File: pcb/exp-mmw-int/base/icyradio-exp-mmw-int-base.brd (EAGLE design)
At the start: 85.7 x 98.4 mm, 22 parts, among them U1 ATSAMD20E16A-M, U3 24AA02XX-X/OT

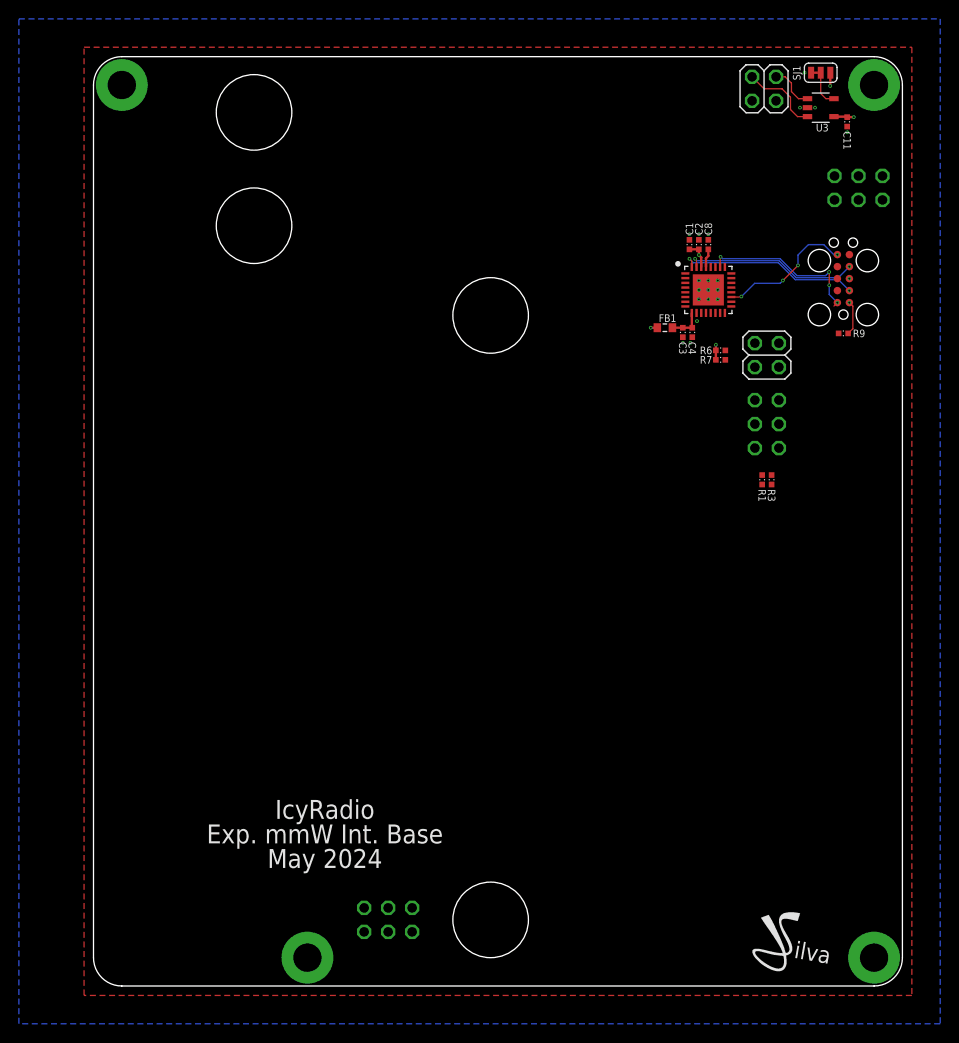
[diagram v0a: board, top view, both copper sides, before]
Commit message: pcb: Finish mmWave integrated expansion PCBs for production
Signed-off-by: João Silva <jgc3silva@gmail.com>
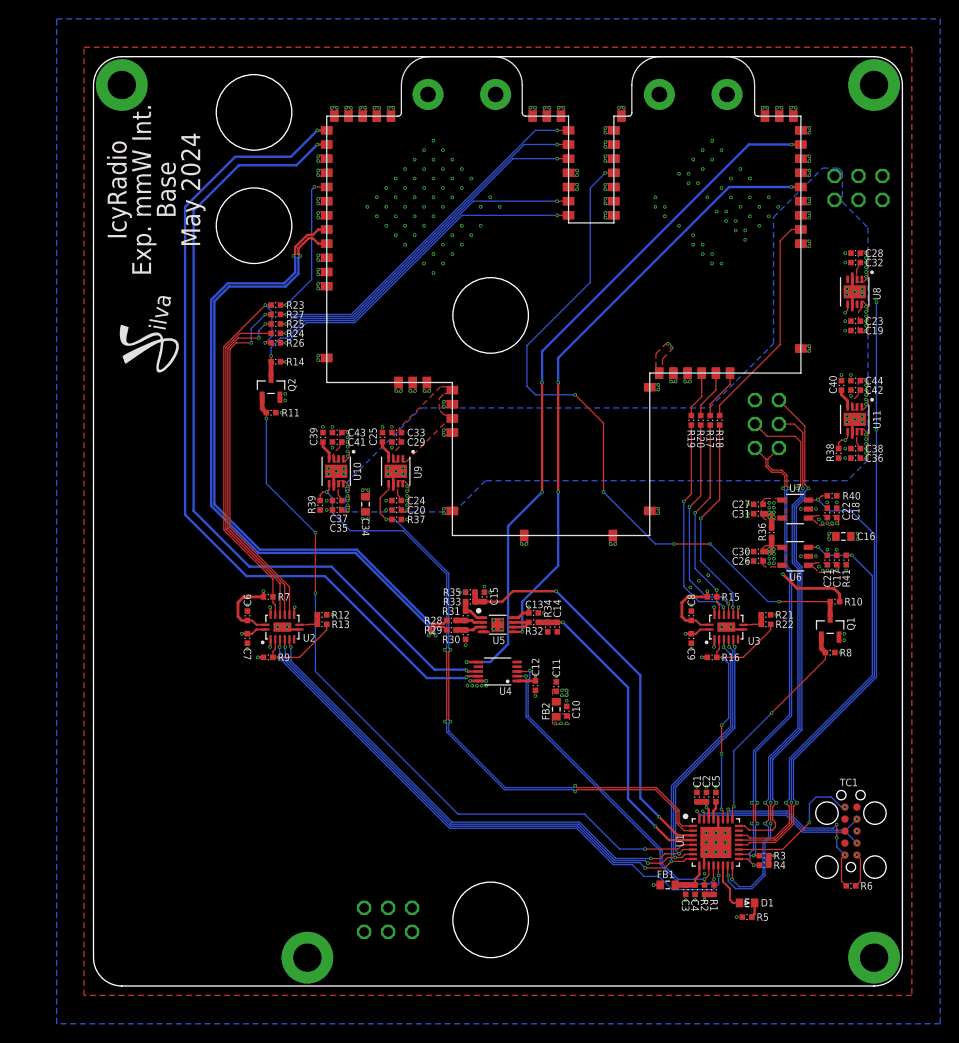
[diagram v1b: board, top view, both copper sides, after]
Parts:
- removed JP5: PINHD-2X3, Pin Header:2X03
- removed JP8, JP9: PINHD-2X2, Pin Header:2X02
- removed SJ1: (no value), Solder Jumper:SJ2C_S
- added C10, C17, C18, C19, C20, C26, C27, C28, C29, C35, C36, C41, C42, C5: 1uF, Capacitor:CAP0402
- added C12, C13, C21, C22, C23, C24, C37, C38, C6, C7, C9: 100nF, Capacitor:CAP0402
- added C14: 1nF, Capacitor:CAP0402
- added C15: 330pF, Capacitor:CAP0402
- added C16, C34: 10uF, Capacitor:CAP0603
- added C25, C39, C40: 10nF, Capacitor:CAP0402
- added C30, C31, C32, C33, C43, C44: 10uF, Capacitor:CAP0402
- added D1: LED0603, LED:0603
- added FB2: 1uH, Inductor:IND0603
- added JP1: PINHD-2X3, Pin Header:2X03
- added P1, P10, P11, P12, P13, P14, P15, P16, P17, P18, P19, P2, P20, P21, P22, P23, P24, P25, P26, P27, P28, P29, P3, P30, P31, P32, P33, P34, P35, P36, P37, P38, P39, P4, P40, P41, P42, P43, P44, P45, P46, P47, P48, P49, P5, P50, P51, P52, P53, P54, P55, P56, P57, P58, P59, P6, P60, P61, P62, P63, P64, P65, P66, P67, P7, P8, P9: CHOLE-0.9MM-LAND, PADs:CAST_HOLE_0P9MM_LAND
- added Q1, Q2: AO3400, Alpha Omega:SOT23
- added R10, R11, R14, R15, R16, R37, R38, R39, R40, R41, R8: 10K Ohms, Resistor:RES0402
- added R12, R21, R35: DNP, Resistor:RES0402
- added R13, R22, R36: 0 Ohms, Resistor:RES0402
- added R17, R18, R19, R20, R23, R24, R25, R26, R27: 22 Ohms, Resistor:RES0402
- added R2, R30, R31, R4: 4.7K Ohms, Resistor:RES0402
- added R28, R29, R34, R5: 1K Ohms, Resistor:RES0402
- added R32, R33: 2K Ohms, Resistor:RES0402
- added U10, U11: ADM7171ACPZ-3.3, Analog Devices:LFCSP8_3X3
- added U2: FXL4TD245BQX, ON Semiconductor:DQFN16
- added U4: MCP4728-A0, Microchip:MSOP10
- added U5: MCP6V32-E/MNY, Microchip:TDFN8
- added U6, U7: ADP7142AUJZ-1.8, Analog Devices:SOT23-5
- added U8: ADP7102ACPZ-1.5, Analog Devices:LFCSP8_3X3
- added U9: ADM7171ACPZ-5.0, Analog Devices:LFCSP8_3X3
- C11: value 100nF -> 10uF
- C2: value 10uF -> 1uF
- C8: value 1uF -> 100nF
- R6, R7: value 4.7K Ohms -> 10K Ohms
- U1: value ATSAMD20E16A-M -> ATSAMD21E18A-M
- U3: value 24AA02XX-X/OT -> FXL4TD245BQX; device Microchip:SOT23-5 -> ON Semiconductor:DQFN16
- moved LOGO1 95.4 mm to (2.60, 70.2), turned to 90 degrees
- moved R9 69.9 mm to (18.5, 34.8), turned to 180 degrees
- moved C11 67.3 mm to (49.0, 31.7), turned to 90 degrees
- moved JP2 66.1 mm to (31.2, 7.00), turned to 0 degrees
- moved C3 59.0 mm to (62.7, 10.2)
- moved C4 59.0 mm to (63.7, 10.2)
- moved FB1 59.0 mm to (60.8, 10.7)
- moved TC1 58.5 mm to (80.2, 16.4)
- moved C1 58.5 mm to (63.9, 20.0)
- moved C2 58.5 mm to (64.9, 20.0)
- moved U1 58.5 mm to (65.9, 15.2)
- moved R6 58.4 mm to (80.2, 10.6), turned to 0 degrees
- moved U3 55.9 mm to (67.0, 38.0), turned to 90 degrees
- moved R7 54.1 mm to (18.5, 41.2)
- moved R1 43.7 mm to (65.7, 10.2)
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- renumbered JP4 to JP3
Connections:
- net MCU_SWCLK renamed SWCLK
- net MCU_SWDIO renamed SWDIO
- removed net EE_I2C_SCL: JP8.4, U3.1
- removed net EE_I2C_SDA: JP8.2, U3.3
- removed net EE_WP: SJ1.2, U3.5
- removed net EXT_IO_1_1: JP2.2, JP9.3, R3.1
- removed net EXT_IO_1_2: JP2.1, JP9.1, R1.1
- new net !RX_RST_1V8: P1.PAD_T, Q1.3, R10.1
- new net !RX_SPI_CS: R16.1, R22.1, U1.27, U3.3
- new net !RX_SPI_CS_1V8: R15.1, R17.2, U3.14
- new net !RX_SPI_OE: R21.1, R22.2, U3.9
- new net !TX_RST_1V8: P35.PAD_T, Q2.3, R14.1
- new net !TX_SPI_CS: R13.1, R9.1, U1.13, U2.3
- new net !TX_SPI_CS_1V8: R23.2, R26.2, R7.1, U2.14
- new net !TX_SPI_OE: R12.1, R13.2, U2.9
- new net 1V5_RF_RX: C28.1, C32.1, P57.PAD_T, U8.1, U8.2
- new net 1V8_RF_RX: C27.1, C31.1, C8.1, P58.PAD_T, P59.PAD_T, R10.2, R15.2, R36.2, U3.16, U7.4, U7.5
- new net 1V8_RF_TX: C26.1, C30.1, C6.1, P49.PAD_T, P50.PAD_T, R14.2, R36.1, R7.2, U2.16, U6.4, U6.5
- new net 3V3_DAC_OPA: C11.1, C12.1, C13.1, FB2.2, U4.1, U5.8
- new net 3V3_RF_RX: C42.1, C44.1, P60.PAD_T, P61.PAD_T, P62.PAD_T, P63.PAD_T, P64.PAD_T, P65.PAD_T, U11.1, U11.2, U11.3
- new net 3V3_RF_TX: C41.1, C43.1, P51.PAD_T, P52.PAD_T, P53.PAD_T, P54.PAD_T, P55.PAD_T, P56.PAD_T, U10.1, U10.2, U10.3
- new net 5V0_RF_LO: C29.1, C33.1, P66.PAD_T, P67.PAD_T, U9.1, U9.2, U9.3
- new net DAC_I2C_SCL: R1.1, U1.12, U4.2
- new net DAC_I2C_SDA: R2.1, U1.11, U4.3
- new net LED: D1.A, U1.14
- new net LO_ANA_PWR_EN: R37.2, U1.1, U9.5
- new net N$10: P5.PAD_T, R20.1
- new net N$11: P37.PAD_T, R26.1
- new net N$12: P36.PAD_T, R23.1
- new net N$13: P38.PAD_T, R24.1
- new net N$14: P39.PAD_T, R27.1
- new net N$15: P40.PAD_T, R25.1
- new net N$16: D1.C, R5.2
- new net N$2: C40.1, U11.4
- new net N$3: C25.1, U9.4
- new net N$4: R28.1, R31.2, U5.2
- new net N$5: R29.1, R30.2, U5.3
- new net N$6: R32.2, U5.6, U5.7
- new net N$7: P2.PAD_T, R17.1
- new net N$8: P3.PAD_T, R19.1
- new net N$9: P4.PAD_T, R18.1
- new net N$96: C39.1, U10.4
- new net RF_SPI_MISO: U1.6, U2.6, U3.6
- new net RF_SPI_MOSI: U1.7, U2.5, U3.5
- new net RF_SPI_SCK: U1.8, U2.4, U3.4
- new net RX_ANA_PWR_EN: R38.2, U1.20, U11.5, U8.5
- new net RX_DIG_PWR_EN: R40.2, U1.21, U7.3
- new net RX_GAIN_VCTRL: P44.PAD_T, U4.6
- new net RX_PWR_VDET: P43.PAD_T, U5.5
- new net RX_PWR_VDET_DIV: C14.1, R32.1, R34.2, U1.4
- new net RX_RST: Q1.1, R8.2, U1.25
- new net RX_SPI_MISO_1V8: R18.2, U3.11
- new net RX_SPI_MOSI_1V8: R20.2, U3.12
- new net RX_SPI_SCK_1V8: R19.2, U3.13
- new net TX_ANA_PWR_EN: R39.2, U1.2, U10.5
- new net TX_DIG_PWR_EN: R41.2, U1.22, U6.3
- new net TX_GAIN_VCTRL1: P45.PAD_T, U4.9
- new net TX_GAIN_VCTRL2: P46.PAD_T, U4.8
- new net TX_PWR_VDET: R31.1, R33.2, U5.1
- new net TX_PWR_VDET_DIV: C15.1, R33.1, R35.2, U1.3
- new net TX_PWR_VDET_N: P48.PAD_T, R28.2
- new net TX_PWR_VDET_P: P47.PAD_T, R29.2
- new net TX_RST: Q2.1, R11.2, U1.5
- new net TX_SPI_MISO_1V8: R27.2, U2.11
- new net TX_SPI_MOSI_1V8: R25.2, U2.12
- new net TX_SPI_SCK_1V8: R24.2, U2.13
- net !MCU_RESET: now also R6.1; no longer R9.1
- net 3V3: now also C10.1, C16.1, C17.1, C18.1, C19.1, C21.1, C22.1, C23.1, C7.1, C9.1, FB2.1, R16.2, R2.2, R4.2, U2.1, U2.10, U2.15, U2.2, U3.1, U3.10, U3.15, U3.2, U6.1, U7.1, U8.8; no longer C11.1, R7.2, SJ1.3, U3.4
- net 5V0: now also C20.1, C24.1, C34.1, C35.1, C36.1, C37.1, C38.1, U10.7, U10.8, U11.7, U11.8, U9.7, U9.8
- net EXT_CLK_2_3: now also JP2.3; no longer JP5.3
- net EXT_IO_1_3: now also JP1.4, U1.15; no longer JP2.4
- net EXT_IO_1_4: now also JP1.3, U1.16; no longer JP2.3
- net EXT_IO_1_5: now also JP1.6, U1.24; no longer JP2.6
- net EXT_IO_2_2: now also JP2.6; no longer JP5.6
- net EXT_IO_2_4: now also JP2.4; no longer JP5.4
- net EXT_IO_2_6: now also JP2.2; no longer JP5.2
- net GND: now also C10.2, C12.2, C13.2, C14.2, C15.2, C16.2, C17.2, C18.2, C19.2, C20.2, C21.2, C22.2, C23.2, C24.2, C25.2, C26.2, C27.2, C28.2, C29.2, C30.2, C31.2, C32.2, C33.2, C34.2, C35.2, C36.2, C37.2, C38.2, C39.2, C40.2, C41.2, C42.2, C43.2, C44.2, C5.2, C6.2, C7.2, C9.2, JP1.5, JP2.1, P10.PAD_T, P11.PAD_T, P12.PAD_T, P13.PAD_T, P14.PAD_T, P15.PAD_T, P16.PAD_T, P17.PAD_T, P18.PAD_T, P19.PAD_T, P20.PAD_T, P21.PAD_T, P22.PAD_T, P23.PAD_T, P24.PAD_T, P25.PAD_T, P26.PAD_T, P27.PAD_T, P28.PAD_T, P29.PAD_T, P30.PAD_T, P31.PAD_T, P32.PAD_T, P33.PAD_T, P34.PAD_T, P41.PAD_T, P42.PAD_T, P6.PAD_T, P7.PAD_T, P8.PAD_T, P9.PAD_T, Q1.2, Q2.2, R11.1, R12.2, R21.2, R30.1, R34.1, R35.1, R37.1, R38.1, R39.1, R40.1, R41.1, R5.1, R8.1, U10.6, U10.9, U11.6, U11.9, U2.17, U2.7, U2.8, U3.17, U3.7, U3.8, U4.10, U4.4, U5.4, U5.9, U6.2, U7.2, U8.3, U8.6, U8.9, U9.6, U9.9; no longer JP5.1, JP5.5, SJ1.1, U3.2
- net MCU_I2C_SCL: now also JP1.2, R3.1; no longer JP9.4, R6.1
- net MCU_I2C_SDA: now also JP1.1, R4.1; no longer JP9.2, R7.1
- net N$1: now also C5.1; no longer C8.1
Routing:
- net TX_GAIN_VCTRL1: track 0.00 -> 89.3 mm, vias 0 -> 2
- net TX_GAIN_VCTRL2: track 0.00 -> 86.0 mm, vias 0 -> 2
- net RF_SPI_SCK: track 0.00 -> 81.6 mm, vias 0 -> 4
- net RF_SPI_MOSI: track 0.00 -> 80.5 mm, vias 0 -> 4
- net RF_SPI_MISO: track 0.00 -> 79.5 mm, vias 0 -> 4
- net TX_RST: track 0.00 -> 79.3 mm, vias 0 -> 4
- net RX_ANA_PWR_EN: track 0.00 -> 76.8 mm, vias 0 -> 5
- net RX_GAIN_VCTRL: track 0.00 -> 75.4 mm, vias 0 -> 4
- net !RX_RST_1V8: track 0.00 -> 74.4 mm, vias 0 -> 6
- net TX_PWR_VDET_N: track 0.00 -> 71.3 mm, vias 0 -> 2
- net TX_PWR_VDET_P: track 0.00 -> 70.2 mm, vias 0 -> 2
- net !TX_SPI_CS: track 0.00 -> 68.5 mm, vias 0 -> 2
- net TX_ANA_PWR_EN: track 0.00 -> 68.0 mm, vias 0 -> 4
- net RX_PWR_VDET: track 0.00 -> 64.9 mm, vias 0 -> 4
- net LO_ANA_PWR_EN: track 0.00 -> 61.9 mm, vias 0 -> 4
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- added copper zone on layer 1, net 1V5_RF_RX
- added copper zone on layer 2, net 1V5_RF_RX
- added copper zone on layer 1, net 1V8_RF_RX
- added copper zone on layer 15, net 1V8_RF_RX
- added copper zone on layer 1, net 1V8_RF_TX
- added copper zone on layer 15, net 1V8_RF_TX
- added copper zone on layer 1, net 3V3
- added copper zone on layer 15, net 3V3
- added copper zone on layer 1, net 3V3_DAC_OPA
- added copper zone on layer 15, net 3V3_DAC_OPA
- added copper zone on layer 1, net 3V3_RF_RX
- added copper zone on layer 15, net 3V3_RF_RX
- added copper zone on layer 1, net 3V3_RF_TX
- added copper zone on layer 15, net 3V3_RF_TX
- added copper zone on layer 1, net 5V0
- added copper zone on layer 16, net 5V0
- added copper zone on layer 1, net 5V0_RF_LO
